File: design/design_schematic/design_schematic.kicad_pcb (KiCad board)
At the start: 4 copper layers, 282.9 x 224.2 mm, 145 parts, among them IC2 XC9148G50CER-G, IC3 nRF52833-QDAA-R7, IC4 74AHCT125PW,118, IC5 MCP23018T-E_SS, IC6 XC9291B33D1R-G, J1 USB_C_Receptacle_USB2.0_16P, J2 Battery Pos, J3 Battery Neg, J4 OLED_128x32, J5 0781271220, U2 BQ24072RGT, U3 USB6B1, U4 BQ27441-G1, U5 PEC11L-4015F-S0015, U6 PEC11L-4015F-S0015, X1 32MHz

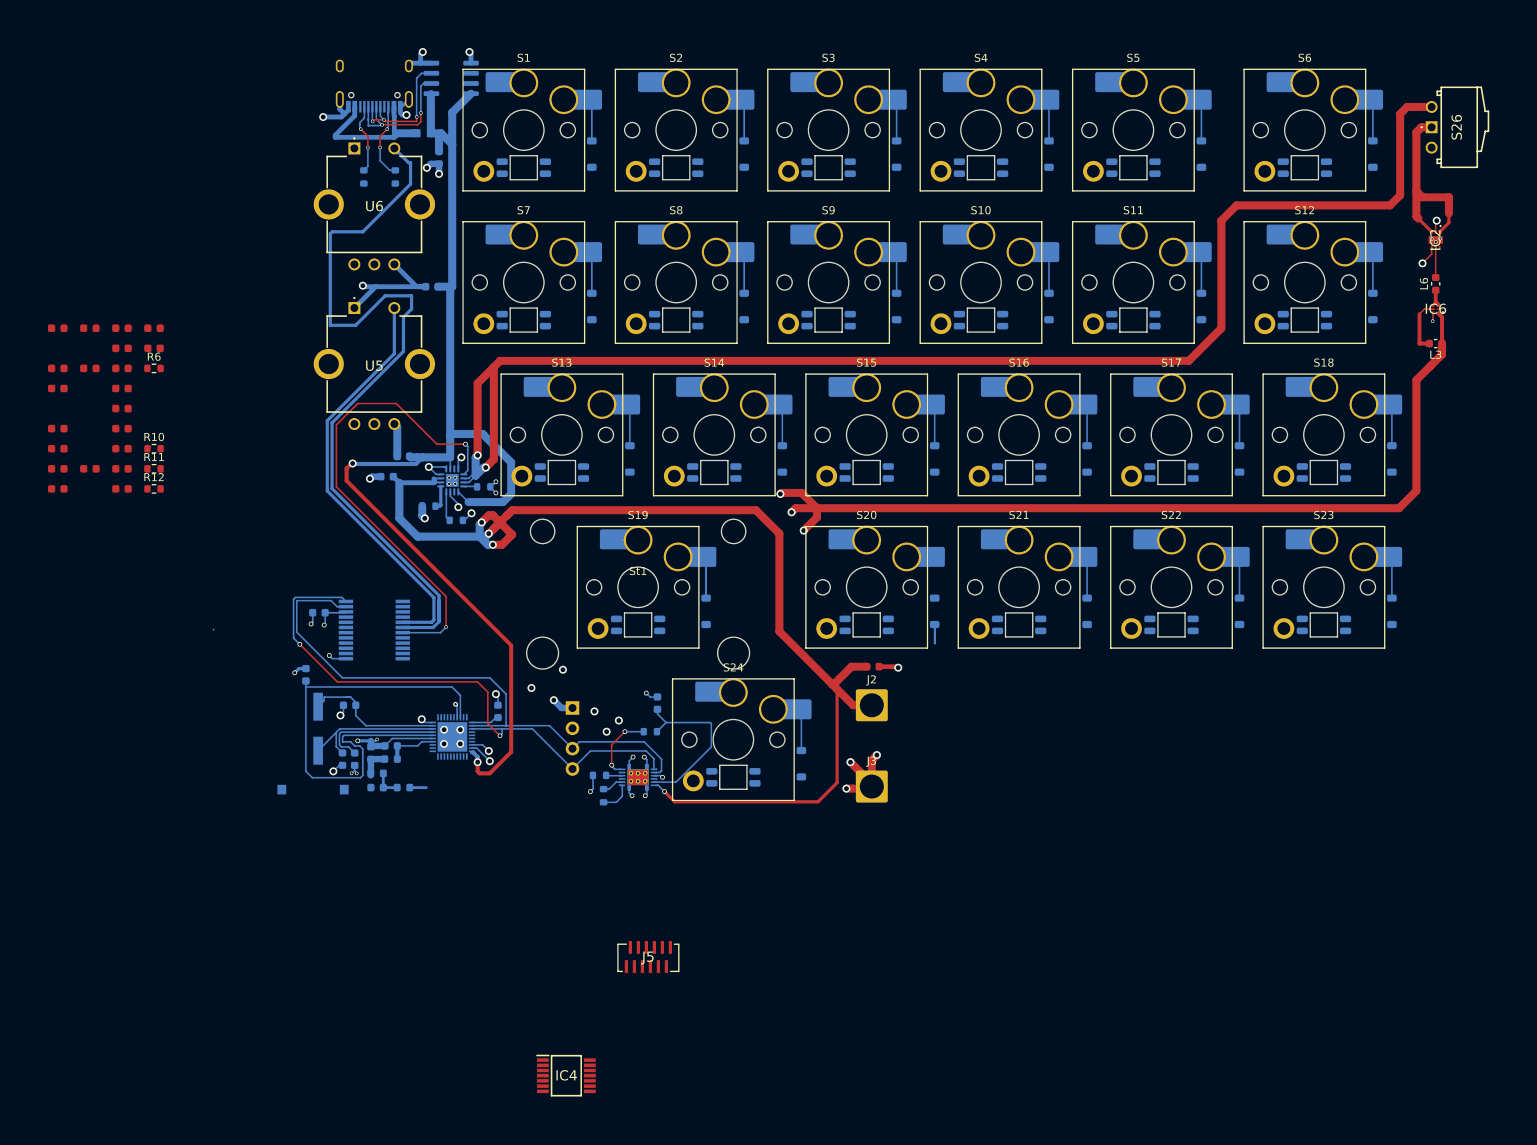
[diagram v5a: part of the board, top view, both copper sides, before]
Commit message: begin to relocate usb c data lines
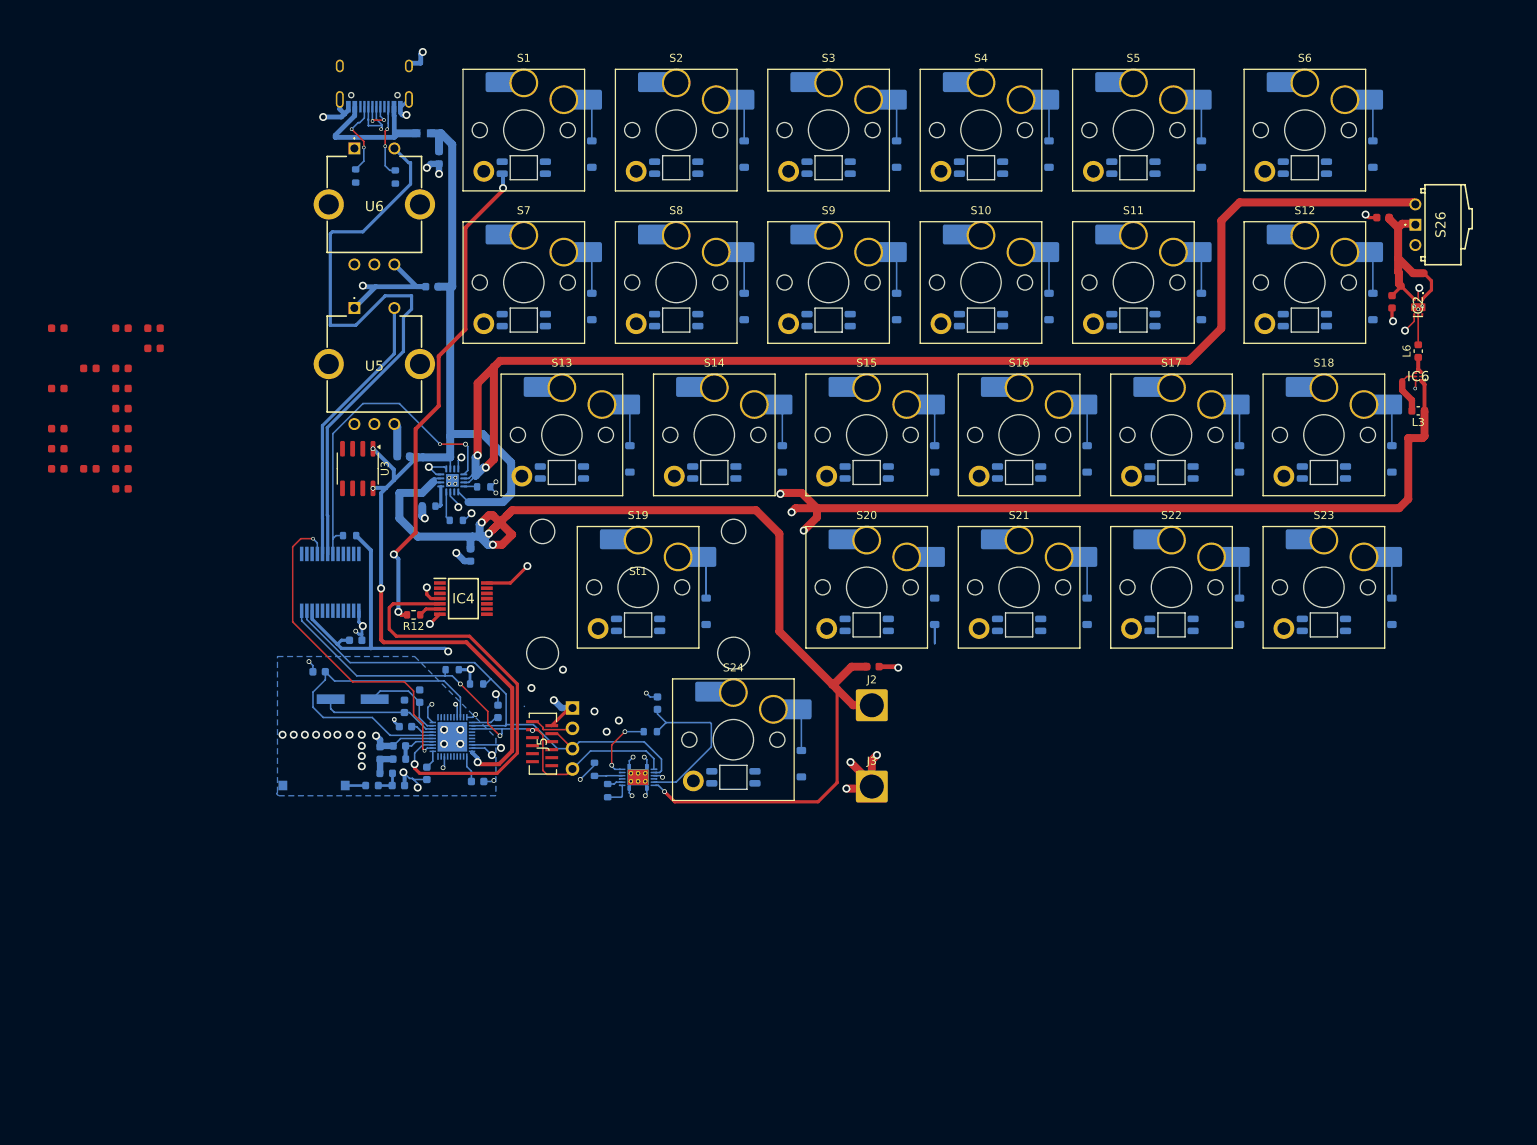
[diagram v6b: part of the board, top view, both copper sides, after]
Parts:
- C11, C4, R10, R11, R6: moved to B.Cu
- U3: moved to F.Cu
- moved C10 168.4 mm to (199.0, 58.0), turned to -90 degrees
- moved C25 158.5 mm to (197.9, 47.5), turned to 180 degrees
- moved C4 73.6 mm to (84.7, 117.9), turned to 180 degrees
- moved C11 69.8 mm to (78.4, 116.9), turned to -90 degrees
- moved IC4 61.0 mm to (82.9, 95.1)
- moved U3 50.1 mm to (69.7, 78.8), turned to -90 degrees
- moved R10 49.9 mm to (84.6, 105.8), turned to 180 degrees
- moved R11 44.9 mm to (81.5, 104.0)
- moved R12 36.1 mm to (76.7, 97.1), turned to 180 degrees
- moved R6 32.2 mm to (68.7, 87.2)
- moved J5 29.5 mm to (91.2, 113.0), turned to 90 degrees
- moved C17 14.3 mm to (83.8, 89.6), turned to -90 degrees
- moved S26 12.3 mm to (201.9, 48.3)
- moved C19 10.2 mm to (75.6, 108.5), turned to 90 degrees
- moved C14 8.84 mm to (77.5, 107.3), turned to 90 degrees
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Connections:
- ANT1 pad 1: (no net) -> Net-(ANT1-FEED)
- ANT1 pad 2: (no net) -> unconnected-(ANT1-NC-Pad2)
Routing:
- net Net-(D1-DIN): track 0.00 -> 61.9 mm, vias 0 -> 3
- net /2A: track 0.00 -> 55.5 mm, vias 0 -> 1
- net /INTA: track 0.00 -> 42.4 mm, vias 0 -> 2
- net 3V3: track 198.0 -> 236.2 mm, vias 12 -> 15
- net /NO2: track 99.0 -> 77.8 mm
- net /CHG: track 60.1 -> 40.8 mm
- net /NO: track 52.0 -> 34.5 mm
- net /DEC4: track 59.5 -> 42.2 mm
- net Net-(S26-NO): track 177.8 -> 165.0 mm
- net Net-(IC3-DEC3): track 15.5 -> 2.92 mm
- net GND: track 120.2 -> 132.6 mm, vias 52 -> 65
- net Net-(J1-D+-PadA6): track 16.6 -> 5.20 mm, vias 3 -> 2
- net Net-(J1-D--PadA7): track 17.8 -> 7.49 mm, vias 2 -> 1
- net /VBUS: track 148.2 -> 139.1 mm, vias 2 -> 4
- net /SDA: track 73.3 -> 65.3 mm, vias 2 -> 3
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- added copper zone on B.Cu, net GND

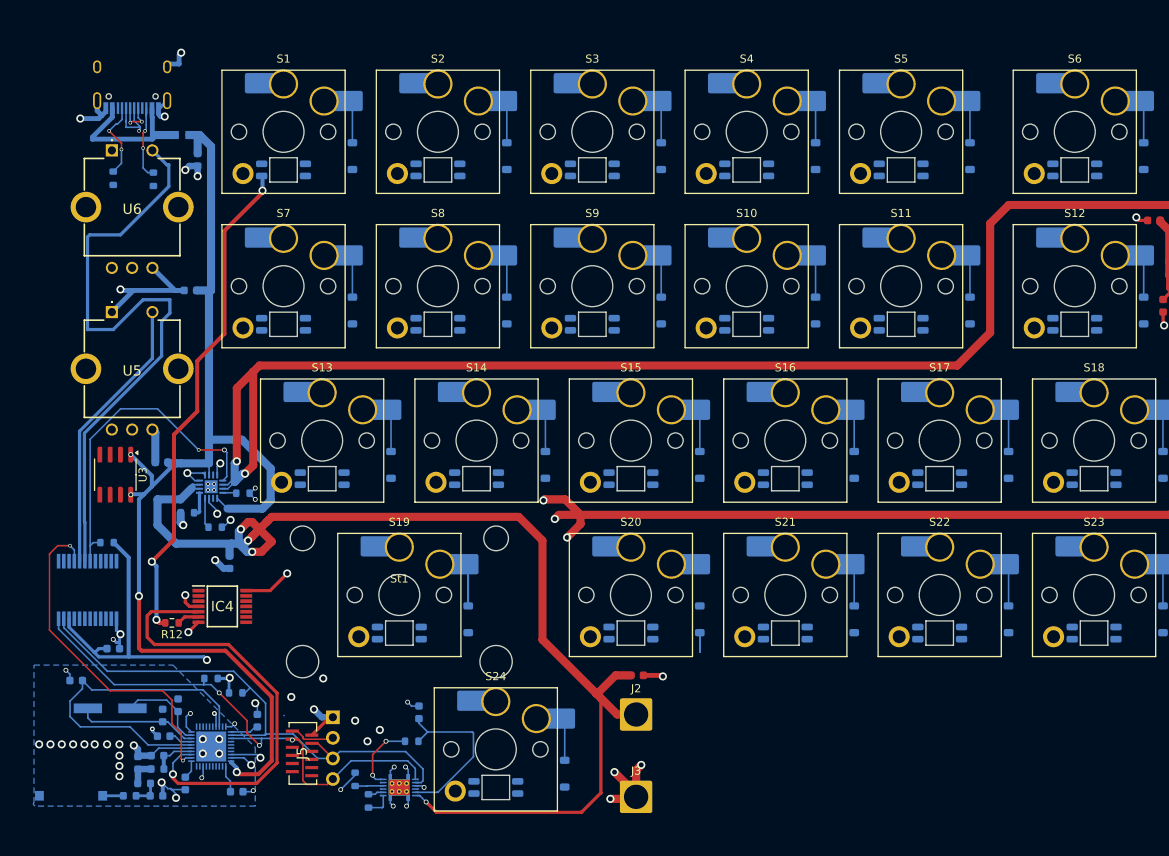
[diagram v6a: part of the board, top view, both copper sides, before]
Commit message: prepare to move around traces for better routing
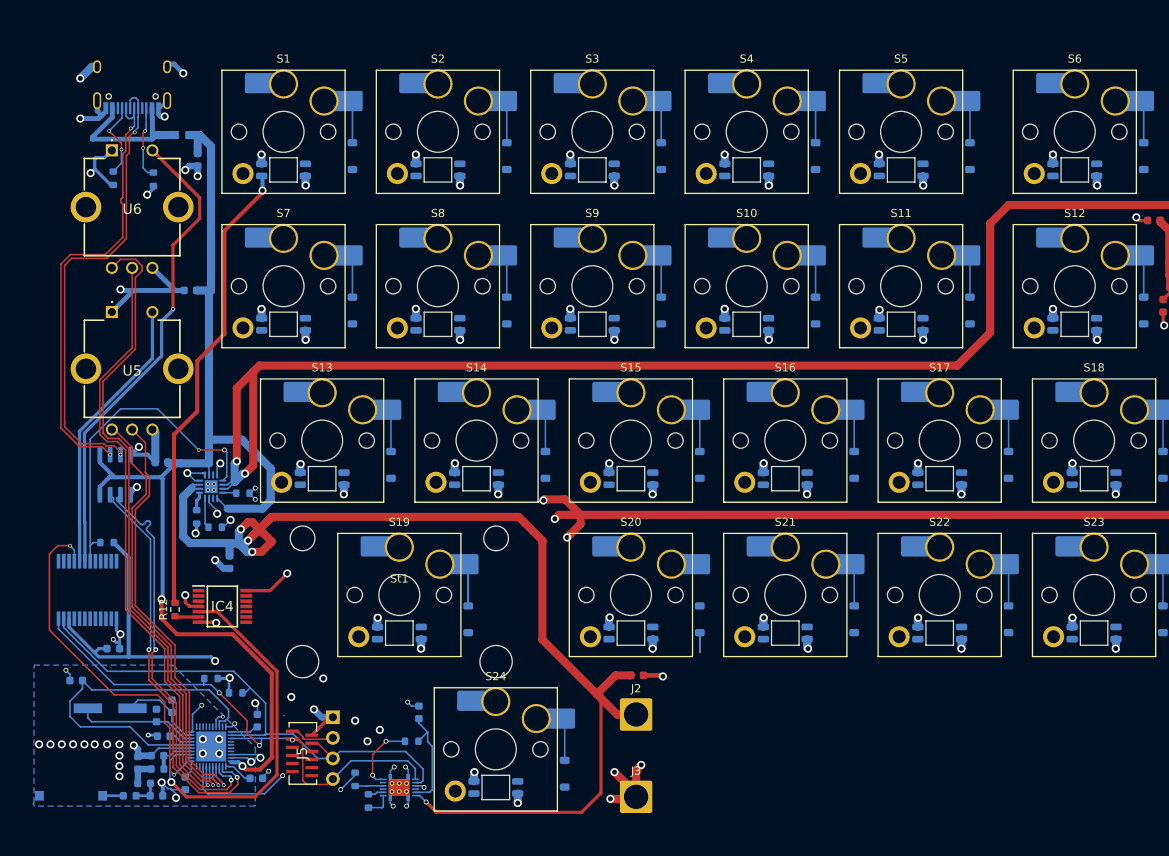
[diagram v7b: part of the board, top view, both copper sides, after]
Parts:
- U3: moved to B.Cu
- moved C4 2.92 mm to (87.1, 116.3)
- moved R12 1.69 mm to (77.1, 95.5), turned to 90 degrees
- moved R5 1.25 mm to (79.8, 84.0), turned to 90 degrees
- moved C14 0.77 mm to (76.7, 107.4)
- moved C19 0.76 mm to (74.8, 108.5)
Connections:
- net Net-(J1-D+-PadA6) renamed /D_P
- net Net-(J1-D--PadA7) renamed /D_N
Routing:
- net /CCW2: track 0.00 -> 80.1 mm, vias 0 -> 1
- net /CW2: track 0.00 -> 74.8 mm, vias 0 -> 1
- net /CCW: track 0.00 -> 54.2 mm, vias 0 -> 1
- net /CW: track 0.00 -> 53.4 mm, vias 0 -> 1
- net /D_P: track 5.20 -> 57.4 mm
- net D-: track 0.00 -> 50.3 mm, vias 0 -> 2
- net D+: track 0.00 -> 50.2 mm, vias 0 -> 2
- net /D_N: track 7.49 -> 56.8 mm, vias 1 -> 2
- net GND: track 132.6 -> 177.7 mm, vias 65 -> 94
- net 5V: track 5.94 -> 34.4 mm, vias 1 -> 25
- net /NO2: track 77.8 -> 59.0 mm, vias 0 -> 1
- net 3V3: track 236.2 -> 250.4 mm
- net /2A: track 55.5 -> 46.1 mm
- net Net-(U4-V_{DD}): track 21.3 -> 13.3 mm
- net Net-(J2-Pin_1): track 145.7 -> 140.4 mm
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
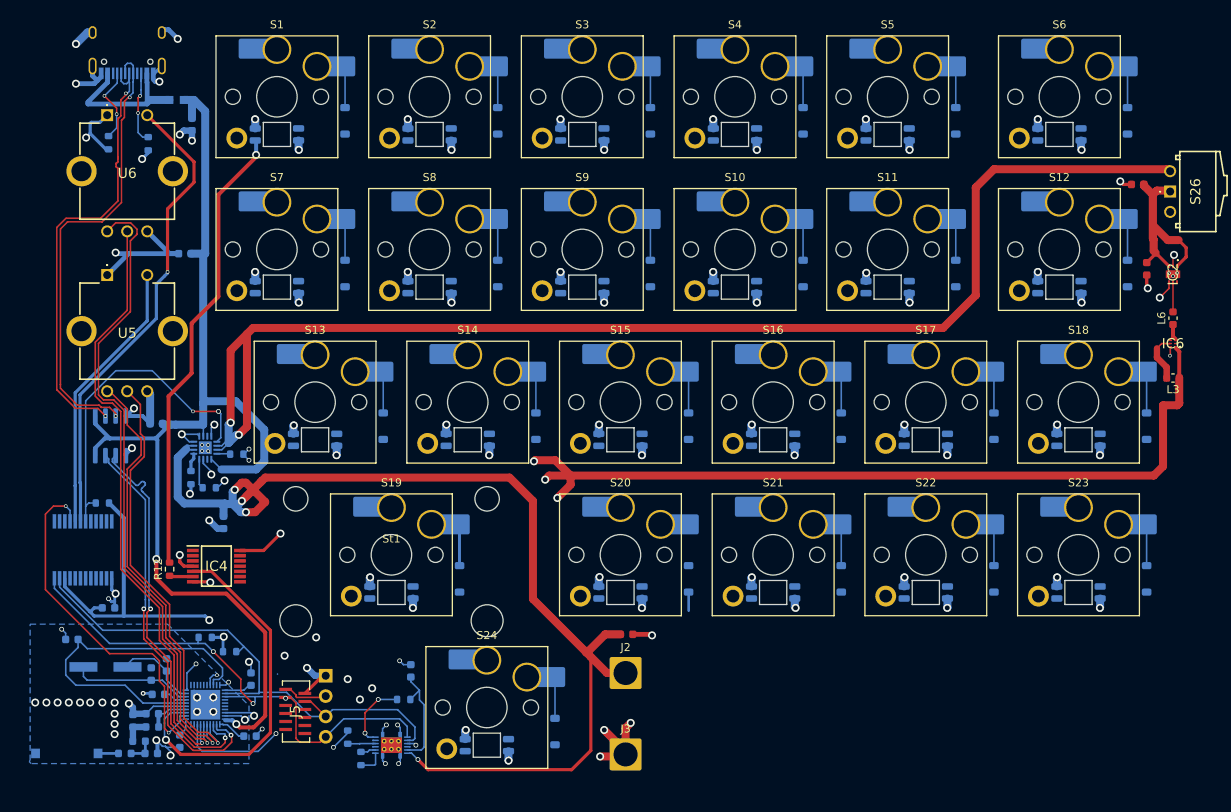
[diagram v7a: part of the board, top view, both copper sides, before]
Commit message: finish switch routing
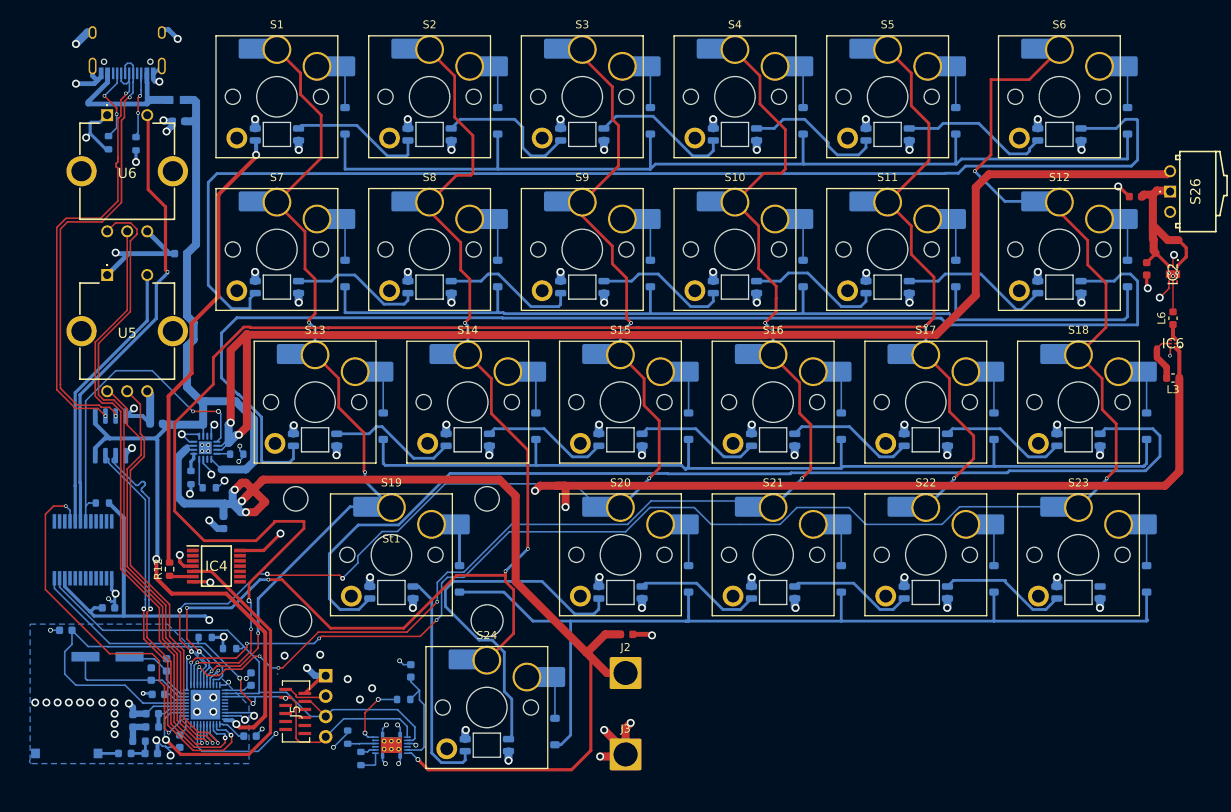
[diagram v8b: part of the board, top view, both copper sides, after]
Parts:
- moved C35 1.71 mm to (78.2, 39.6), turned to 180 degrees
- moved C25 1.55 mm to (197.6, 49.0)
- moved R2 1.52 mm to (72.9, 42.4)
- moved C6 1.37 mm to (64.2, 103.1)
- moved X1 1.30 mm to (69.4, 106.4)
- moved C23 0.51 mm to (78.5, 56.1)
- moved R10 0.38 mm to (84.6, 105.4)
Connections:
- D11 pad 4: Net-(D11-DIN) -> Net-(D10-DOUT)
- D12 pad 4: Net-(D12-DIN) -> Net-(D11-DOUT)
- D13 pad 4: Net-(D13-DIN) -> Net-(D12-DOUT)
- D14 pad 4: Net-(D10-DOUT) -> Net-(D13-DOUT)
- D15 pad 2: Net-(D11-DIN) -> Net-(D15-DOUT)
- D15 pad 4: Net-(D15-DIN) -> Net-(D14-DOUT)
- D16 pad 2: Net-(D12-DIN) -> Net-(D16-DOUT)
- D16 pad 4: Net-(D16-DIN) -> Net-(D15-DOUT)
- D17 pad 4: Net-(D13-DOUT) -> Net-(D16-DOUT)
- D18 pad 4: Net-(D14-DOUT) -> Net-(D17-DOUT)
- D19 pad 2: Net-(D15-DIN) -> Net-(D19-DOUT)
- D19 pad 4: Net-(D19-DIN) -> Net-(D18-DOUT)
- D2 pad 4: Net-(D2-DIN) -> Net-(D1-DOUT)
- D20 pad 2: Net-(D16-DIN) -> Net-(D20-DOUT)
- D21 pad 4: Net-(D17-DOUT) -> Net-(D20-DOUT)
- D22 pad 4: Net-(D18-DOUT) -> Net-(D21-DOUT)
- D23 pad 2: Net-(D19-DIN) -> unconnected-(D23-DOUT-Pad2)
- D23 pad 4: Net-(D21-DOUT) -> Net-(D22-DOUT)
- D24 pad 4: Net-(D22-DOUT) -> Net-(D19-DOUT)
- D3 pad 2: Net-(D2-DIN) -> Net-(D3-DOUT)
- D3 pad 4: Net-(D3-DIN) -> Net-(D2-DOUT)
- D4 pad 2: unconnected-(D4-DOUT-Pad2) -> Net-(D4-DOUT)
- D4 pad 4: Net-(D4-DIN) -> Net-(D3-DOUT)
- D5 pad 4: Net-(D1-DOUT) -> Net-(D4-DOUT)
- D6 pad 2: Net-(D10-DIN) -> Net-(D6-DOUT)
- D6 pad 4: Net-(D2-DOUT) -> Net-(D5-DOUT)
- D7 pad 2: Net-(D3-DIN) -> Net-(D7-DOUT)
- D7 pad 4: Net-(D11-DOUT) -> Net-(D6-DOUT)
- D8 pad 2: Net-(D4-DIN) -> Net-(D8-DOUT)
- D8 pad 4: Net-(D12-DOUT) -> Net-(D7-DOUT)
- D9 pad 2: Net-(D13-DIN) -> Net-(D10-DIN)
- D9 pad 4: Net-(D5-DOUT) -> Net-(D8-DOUT)
- Di10 pad 1: /Row 1 -> /Row 0
- Di13 pad 1: /Row 2 -> /Row 1
- Di14 pad 1: /Row 2 -> /Row 1
- Di15 pad 1: /Row 2 -> /Row 1
- Di19 pad 1: /Row 3 -> /Row 2
- Di3 pad 1: /Row 0 -> /Row 1
- Di4 pad 1: /Row 0 -> /Row 2
- Di5 pad 1: /Row 0 -> /Row 2
- Di6 pad 1: /Row 0 -> /Row 3
- Di7 pad 1: /Row 1 -> /Row 0
- Di8 pad 1: /Row 1 -> /Row 0
- Di9 pad 1: /Row 1 -> /Row 0
- S10 pad 1: /Column 0 -> /Column 3
- S11 pad 1: /Column 1 -> /Column 4
- S12 pad 1: /Column 2 -> /Column 5
- S13 pad 1: /Column 3 -> /Column 0
- S14 pad 1: /Column 3 -> /Column 1
- S15 pad 1: /Column 4 -> /Column 2
- S16 pad 1: /Column 5 -> /Column 3
- S18 pad 1: /Column 0 -> /Column 5
- S19 pad 1: /Column 1 -> /Column 0
- S2 pad 1: /Column 0 -> /Column 1
- S21 pad 1: /Column 5 -> /Column 3
- S22 pad 1: /Column 3 -> /Column 4
- S23 pad 1: /Column 4 -> /Column 5
- S24 pad 1: /Column 5 -> /Column 1
- S3 pad 1: /Column 1 -> /Column 2
- S4 pad 1: /Column 2 -> /Column 3
- S5 pad 1: /Column 1 -> /Column 4
- S6 pad 1: /Column 3 -> /Column 5
- S7 pad 1: /Column 4 -> /Column 0
- S8 pad 1: /Column 5 -> /Column 1
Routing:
- net /Column 4: track 0.00 -> 230.0 mm, vias 0 -> 5
- net /Column 5: track 0.00 -> 202.3 mm, vias 0 -> 6
- net /Column 3: track 0.00 -> 154.1 mm, vias 0 -> 6
- net Net-(D12-DOUT): track 0.00 -> 152.6 mm
- net Net-(D6-DOUT): track 0.00 -> 151.1 mm
- net /Column 1: track 0.00 -> 147.8 mm, vias 0 -> 6
- net /Column 2: track 0.00 -> 140.0 mm, vias 0 -> 6
- net Net-(D18-DOUT): track 0.00 -> 131.1 mm
- net /Row 0: track 0.00 -> 122.0 mm
- net /Row 1: track 0.00 -> 119.3 mm
- net /Row 3: track 7.14 -> 126.1 mm
- net /Row 2: track 0.00 -> 116.3 mm
- net /Column 0: track 0.00 -> 101.9 mm, vias 0 -> 4
- net Net-(D20-DIN): track 0.00 -> 46.1 mm
- net Net-(D19-DOUT): track 0.00 -> 28.1 mm
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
